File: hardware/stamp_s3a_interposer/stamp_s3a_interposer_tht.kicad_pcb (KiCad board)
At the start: 2 copper layers, 110 x 72 mm, 38 parts

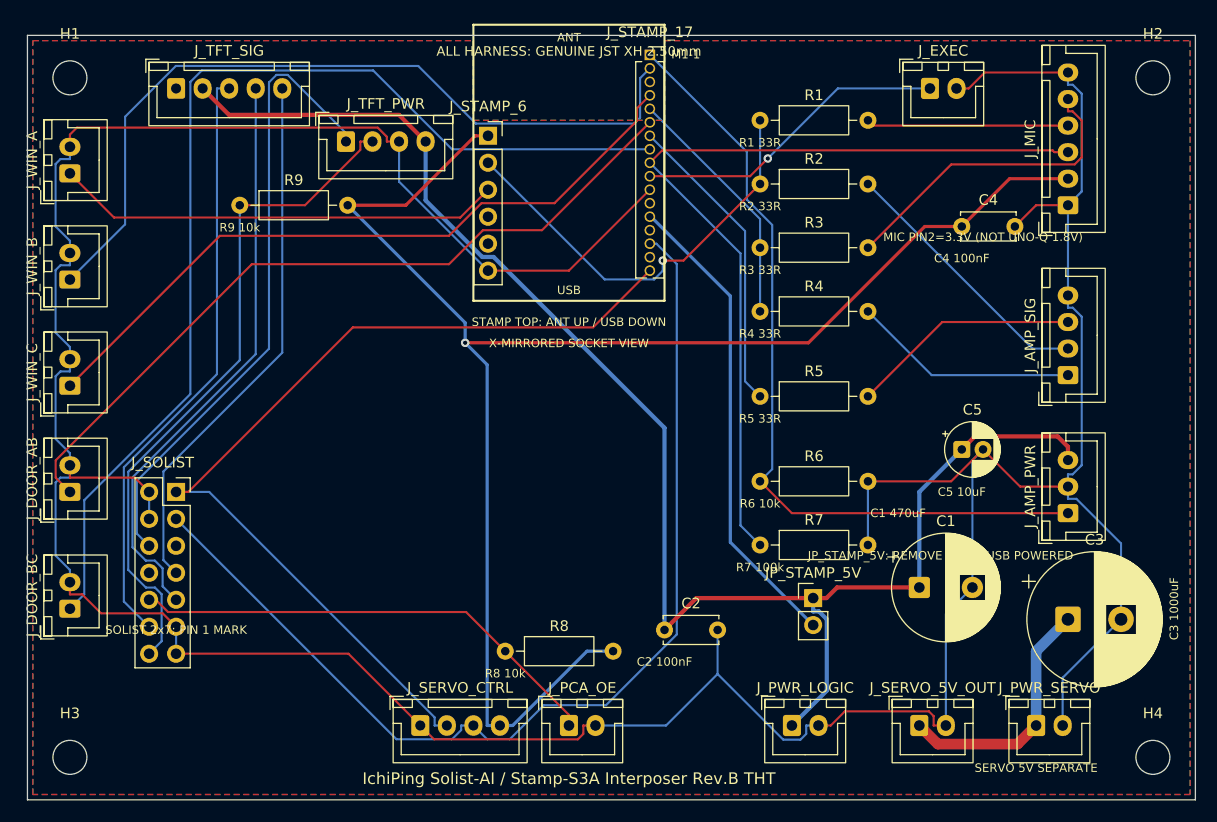
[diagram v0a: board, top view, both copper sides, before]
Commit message: Finalize compact Stamp-S3A interposer manufacturing files
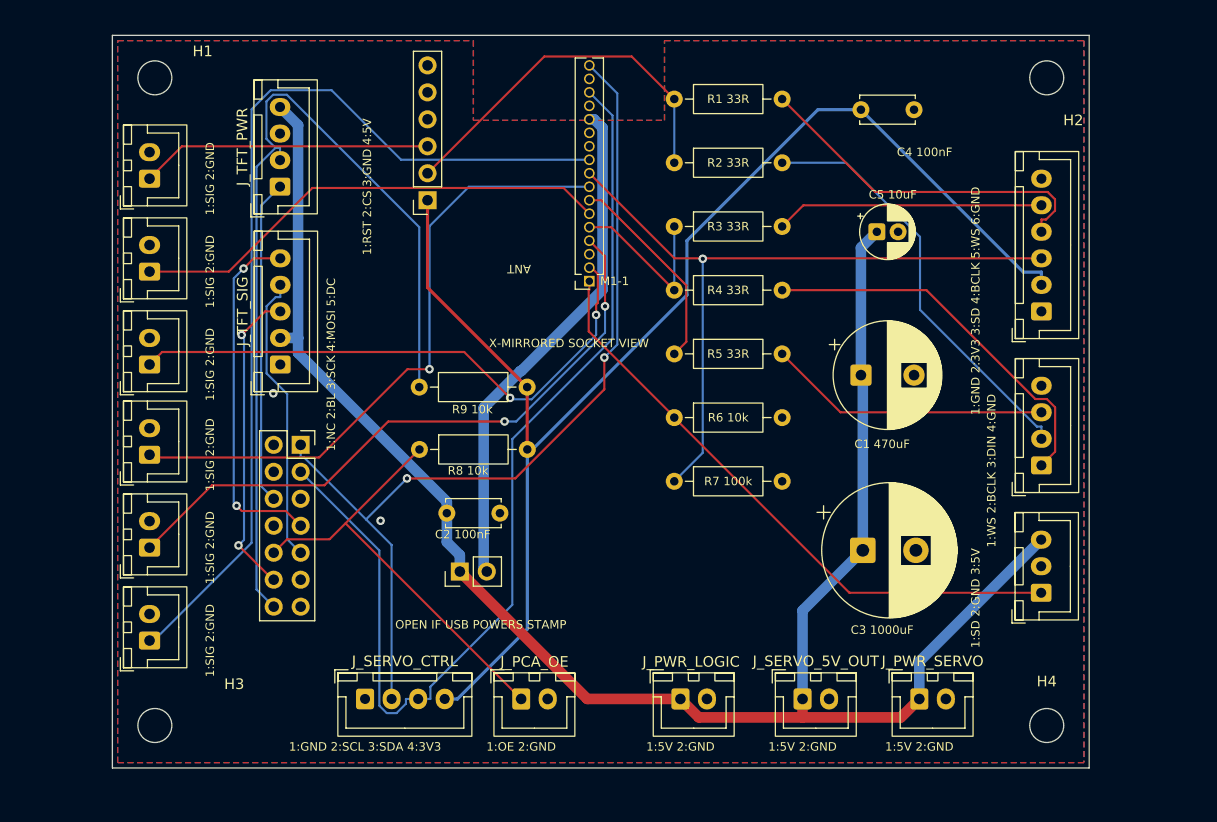
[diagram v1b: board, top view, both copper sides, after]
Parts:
- C1: value 470uF/10V LOGIC -> 470uF/16V LOGIC
- C3: value 1000uF/10V SERVO -> 1000uF/35V SERVO
- J_AMP_SIG: value AMP:LRC,BCLK,DIN,GAIN -> AMP:LRC,BCLK,DIN,GND
- J_PWR_LOGIC: value INPUT:5V_LOGIC,GND -> INPUT:COMMON_5V,GND
- J_PWR_SERVO: value INPUT:5V_SERVO,GND -> INPUT:COMMON_5V,GND
- J_SERVO_5V_OUT: value SERVO:5V,GND -> SERVO:COMMON_5V,GND
- moved J_EXEC 90.0 mm to (21.5, 67.0), turned to 90 degrees
- moved JP_STAMP_5V 33.4 mm to (50.7, 60.5), turned to 90 degrees
- moved J_TFT_SIG 27.8 mm to (33.8, 41.0), turned to 90 degrees
- moved R9 24.1 mm to (46.9, 43.1)
- moved C2 23.3 mm to (49.5, 55.0)
- moved J_DOOR_AB 22.1 mm to (21.5, 32.2)
- moved J_STAMP_17 22.1 mm to (62.9, 33.1), turned to 180 degrees
- moved C5 22.0 mm to (90.0, 28.5)
- moved C1 20.7 mm to (88.5, 42.0)
- moved R8 20.6 mm to (46.9, 49.0)
- moved C3 20.4 mm to (88.7, 58.5)
- moved J_WIN_C 17.0 mm to (21.5, 58.2)
- moved J_DOOR_BC 16.3 mm to (21.5, 49.5)
- moved C4 14.5 mm to (88.5, 17.0)
- moved J_SOLIST 12.5 mm to (35.7, 48.6)
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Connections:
- C3 pad 1: +5V_SERVO -> +5V_LOGIC
- J_PWR_SERVO pad 1: +5V_SERVO -> +5V_LOGIC
- J_SERVO_5V_OUT pad 1: +5V_SERVO -> +5V_LOGIC
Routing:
- net GND: track 370.9 -> 0.00 mm, vias 0 -> 2
- net EXEC_N: track 29.8 -> 89.5 mm, vias 1 -> 0
- net SW_DOOR_BC: track 101.1 -> 60.0 mm, vias 0 -> 1
- net TFT_RST_N: track 59.9 -> 30.6 mm
- net TFT_MOSI: track 55.2 -> 27.3 mm
- net TFT_SCK: track 56.5 -> 29.4 mm, vias 0 -> 2
- net SW_DOOR_AB: track 72.7 -> 45.7 mm
- net +5V_LOGIC: track 145.7 -> 170.7 mm
- net +5V_SERVO: track 23.7 -> 0.00 mm
- net SW_WIN_B: track 75.5 -> 53.8 mm, vias 0 -> 2
- net TFT_CS_N: track 64.3 -> 85.8 mm
- net +3V3_STAMP: track 148.3 -> 127.0 mm, vias 1 -> 0
- net AMP_SD: track 75.7 -> 57.6 mm
- net TFT_DC: track 50.8 -> 33.5 mm, vias 0 -> 2
- net I2S_WS_AMP: track 21.3 -> 36.3 mm
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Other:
- board size 110 x 72 mm -> 92 x 69 mm
- board text added: "1:5V 2:GND"
- board text added: "1:GND 2:3V3 3:SD 4:BCLK 5:WS 6:GND"
- board text added: "1:GND 2:SCL 3:SDA 4:3V3"
- board text added: "1:NC 2:BL 3:SCK 4:MOSI 5:DC"
- board text added: "1:OE 2:GND"
- board text added: "1:RST 2:CS 3:GND 4:5V"
- board text added: "1:SD 2:GND 3:5V"
- board text added: "1:SIG 2:GND"
- board text added: "1:WS 2:BCLK 3:DIN 4:GND"
- board text added: "J_PWR_LOGIC + J_PWR_SERVO: SAME 5V SUPPLY ONLY"
- board text added: "OPEN IF USB POWERS STAMP"
- board text removed: "ALL HARNESS: GENUINE JST XH 2.50mm"
- board text removed: "JP_STAMP_5V: REMOVE WHEN USB POWERED"
- board text removed: "MIC PIN2=3.3V (NOT UNO-Q 1.8V)"
- board text removed: "SERVO 5V SEPARATE"
- board text removed: "SOLIST 2x7: PIN 1 MARK"
- board text removed: "STAMP TOP: ANT UP / USB DOWN"
- board text removed: "USB"
